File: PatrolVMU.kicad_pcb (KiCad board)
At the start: 2 copper layers, 48 parts, among them J1 C-OBD-II-16M, J2 Conn_01x03_Pin, Q1 BC549CTA, Q2 BC549CTA, U1 ESP32-C3, U2 CD4060BNSR, U3 L7805, U4 LM358ST, U5 INA226, U6 TLV7031DBV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

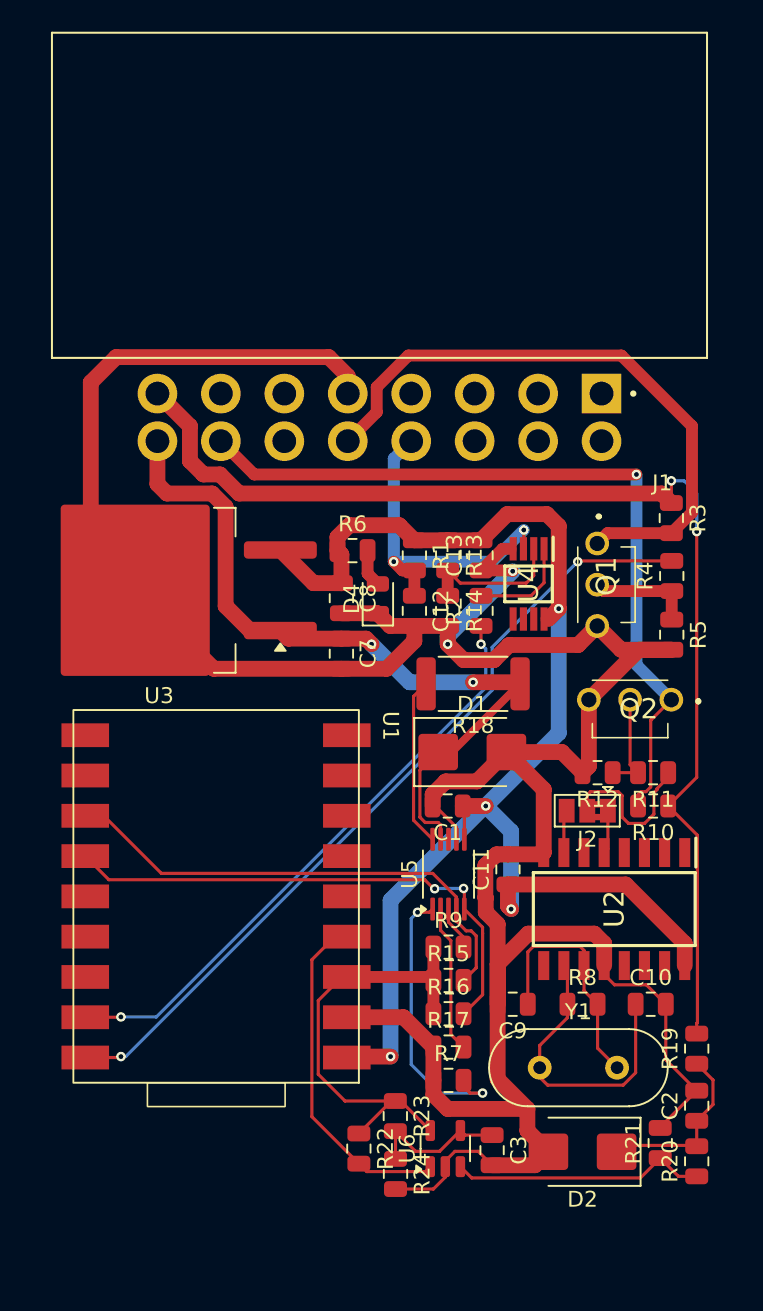
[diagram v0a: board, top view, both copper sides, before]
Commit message: fixed texts, added mt holes, etc
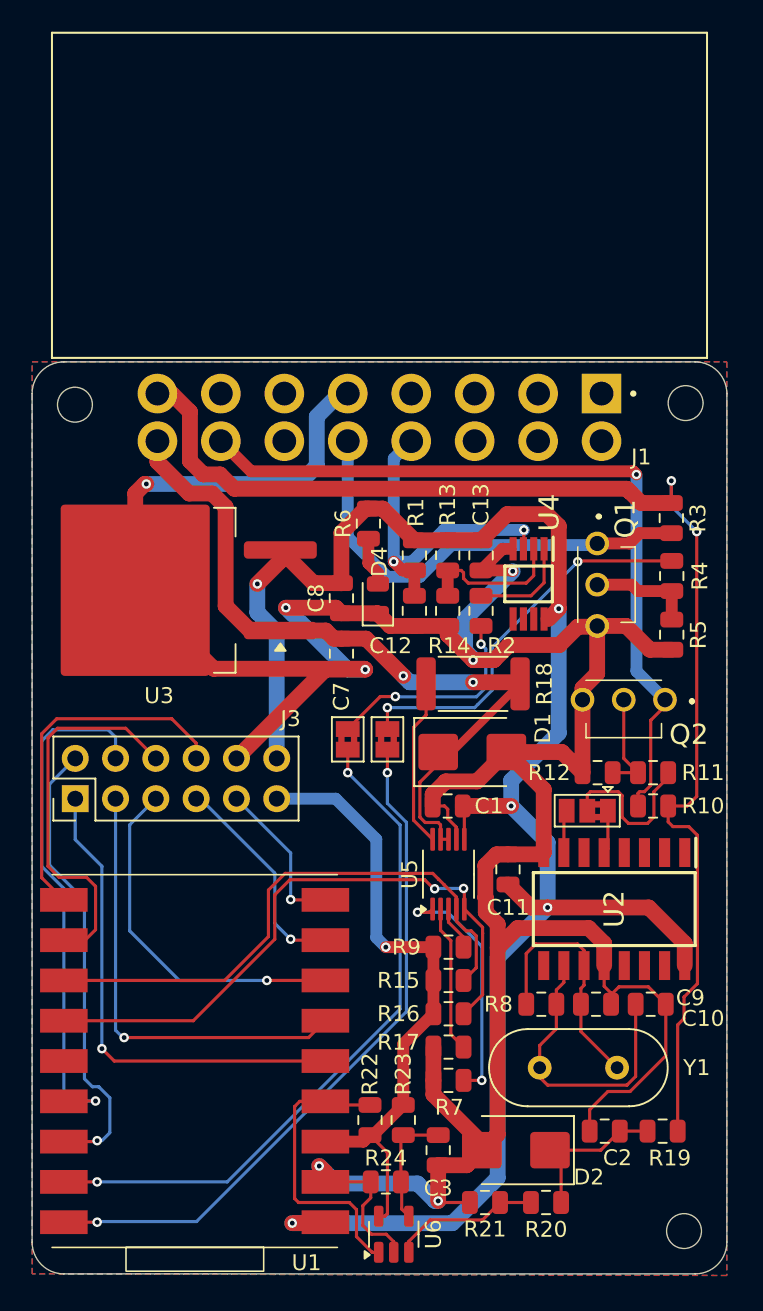
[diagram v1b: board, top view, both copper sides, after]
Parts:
- added H1: MountingHole, MountingHole:MountingHole_2.2mm_M2, F.Cu at (105.9, 85.2)
- added H2: MountingHole, MountingHole:MountingHole_2.2mm_M2, F.Cu at (144.4, 85.1)
- added H3: MountingHole, MountingHole:MountingHole_2.2mm_M2, F.Cu at (144.3, 137.3)
- added J3: Conn_02x06_Odd_Even, Connector_PinHeader_2.54mm:PinHeader_2x06_P2.54mm_Vertical, F.Cu at (105.9, 110.0)
- added JP1: SolderJumper_2_Bridged, Jumper:SolderJumper-2_P1.3mm_Bridged2Bar_Pad1.0x1.5mm, F.Cu at (125.6, 106.3)
- added JP2: SolderJumper_2_Bridged, Jumper:SolderJumper-2_P1.3mm_Bridged2Bar_Pad1.0x1.5mm, F.Cu at (123.1, 106.3)
- moved R21 11.7 mm to (131.8, 135.5), turned to 180 degrees
- moved U1 10.5 mm to (114.0, 126.8)
- moved R20 9.85 mm to (135.6, 135.5), turned to 0 degrees
- moved U6 6.30 mm to (126.0, 137.5)
- moved C2 6.02 mm to (139.3, 131.0), turned to 180 degrees
- moved R19 5.63 mm to (142.9, 131.0), turned to 0 degrees
- moved C9 5.25 mm to (138.8, 123.0), turned to 0 degrees
- moved D2 4.20 mm to (133.7, 132.2)
- moved C3 3.40 mm to (128.8, 132.2)
- moved R8 2.60 mm to (135.3, 123.0), turned to 180 degrees
- moved R6 1.97 mm to (124.4, 92.7), turned to -90 degrees
- moved R22 1.93 mm to (124.5, 130.3), turned to 90 degrees
- moved R24 0.79 mm to (125.5, 134.2), turned to 180 degrees
- moved R23 0.56 mm to (126.6, 130.3)
- moved Q2 0.40 mm to (141.4, 104.4)
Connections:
- net +3.3V renamed 3V3
- net +5V renamed 5V
- U1 pad 10: unconnected-(U1-IO6-Pad10) -> ESP_IO6
- U1 pad 11: unconnected-(U1-IO7-Pad11) -> ESP_IO7
- U1 pad 17: ESP_Rx -> Net-(JP2-A)
- U1 pad 18: ESP_Tx -> Net-(JP1-A)
- U1 pad 5: unconnected-(U1-IO1-Pad5) -> ESP_IO1
- U1 pad 6: unconnected-(U1-IO2-Pad6) -> ESP_IO2
- U1 pad 7: unconnected-(U1-IO3-Pad7) -> ESP_IO3
- U1 pad 8: unconnected-(U1-IO4-Pad8) -> ESP_IO4
- U1 pad 9: unconnected-(U1-IO5-Pad9) -> ESP_IO5
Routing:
- net Net-(JP1-A): track 0.00 -> 44.1 mm, vias 0 -> 2
- net Net-(JP2-A): track 0.00 -> 43.4 mm, vias 0 -> 2
- net ESP_USB_D-: track 0.00 -> 33.5 mm, vias 0 -> 1
- net ESP_IO1: track 0.00 -> 31.9 mm, vias 0 -> 1
- net ESP_USB_D+: track 0.00 -> 29.2 mm, vias 0 -> 1
- net ESP_IO2: track 0.00 -> 28.5 mm, vias 0 -> 1
- net 5V: track 91.4 -> 119.3 mm, vias 4 -> 5
- net ESP_Tx: track 51.5 -> 24.7 mm
- net ESP_IO7: track 0.00 -> 24.5 mm
- net ESP_Rx: track 37.9 -> 13.8 mm
- net ESP_IO6: track 0.00 -> 22.8 mm
- net ESP_IO3: track 0.00 -> 22.7 mm, vias 0 -> 1
- net ESP_IO4: track 0.00 -> 13.7 mm, vias 0 -> 1
- net GND: track 200.2 -> 212.8 mm, vias 2 -> 7
- net 3V3: track 28.5 -> 40.6 mm, vias 0 -> 1
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- added copper zone on B.Cu, net GND
- added copper zone on F.Cu, net GND
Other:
- board outline added: 43.8 x 57.5 mm
